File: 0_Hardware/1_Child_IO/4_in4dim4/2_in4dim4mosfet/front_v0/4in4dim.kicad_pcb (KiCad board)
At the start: 2 copper layers, 100.1 x 41.9 mm, 37 parts, among them IC1 ATTINY48-A, P1 CONN_8X2, P2 CONN_2, P3 CONN_2, P4 CONN_2, P5 CONN_2, Q1 PNP, Q2 PNP, Q3 PNP, Q4 PNP

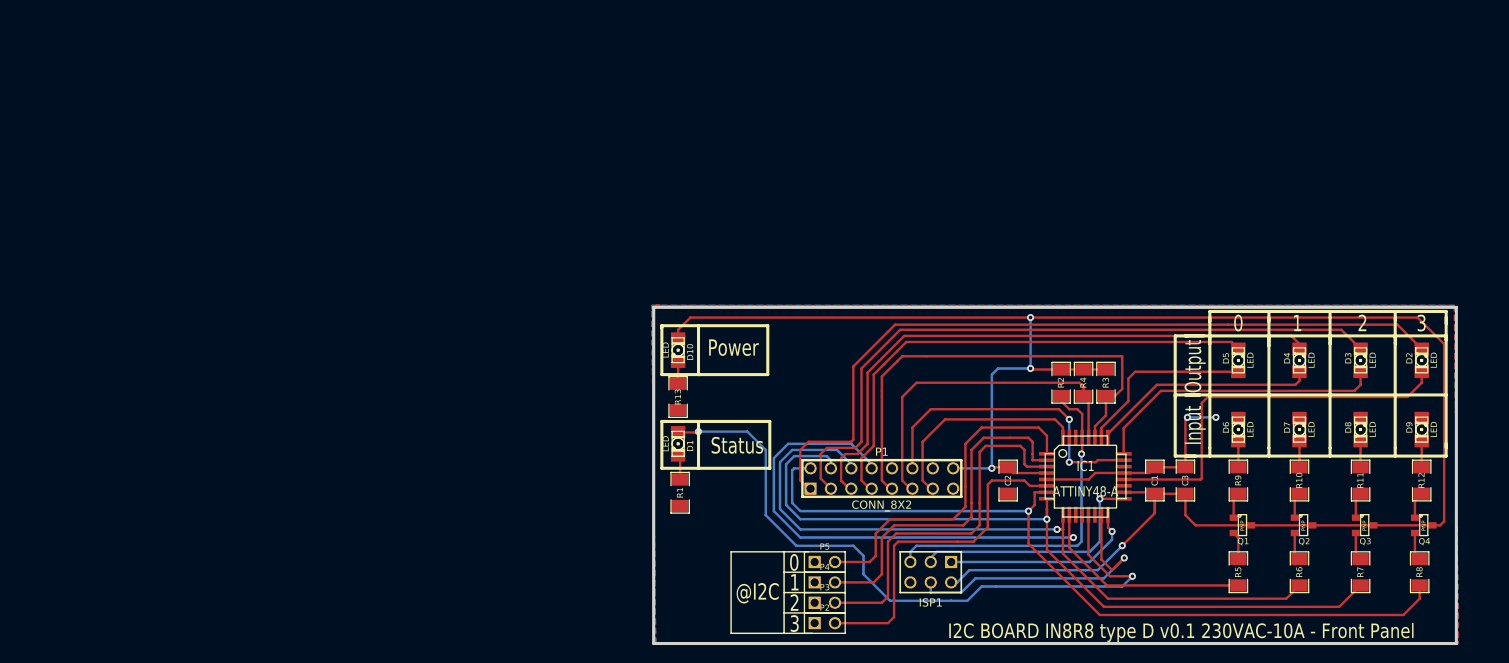
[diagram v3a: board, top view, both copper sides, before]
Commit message: MàJ du pcb front panel in4dim4 mosfet
Décalage vers la gauche des leds pawer status
Décalage vers le haut des cavaliers @I2C
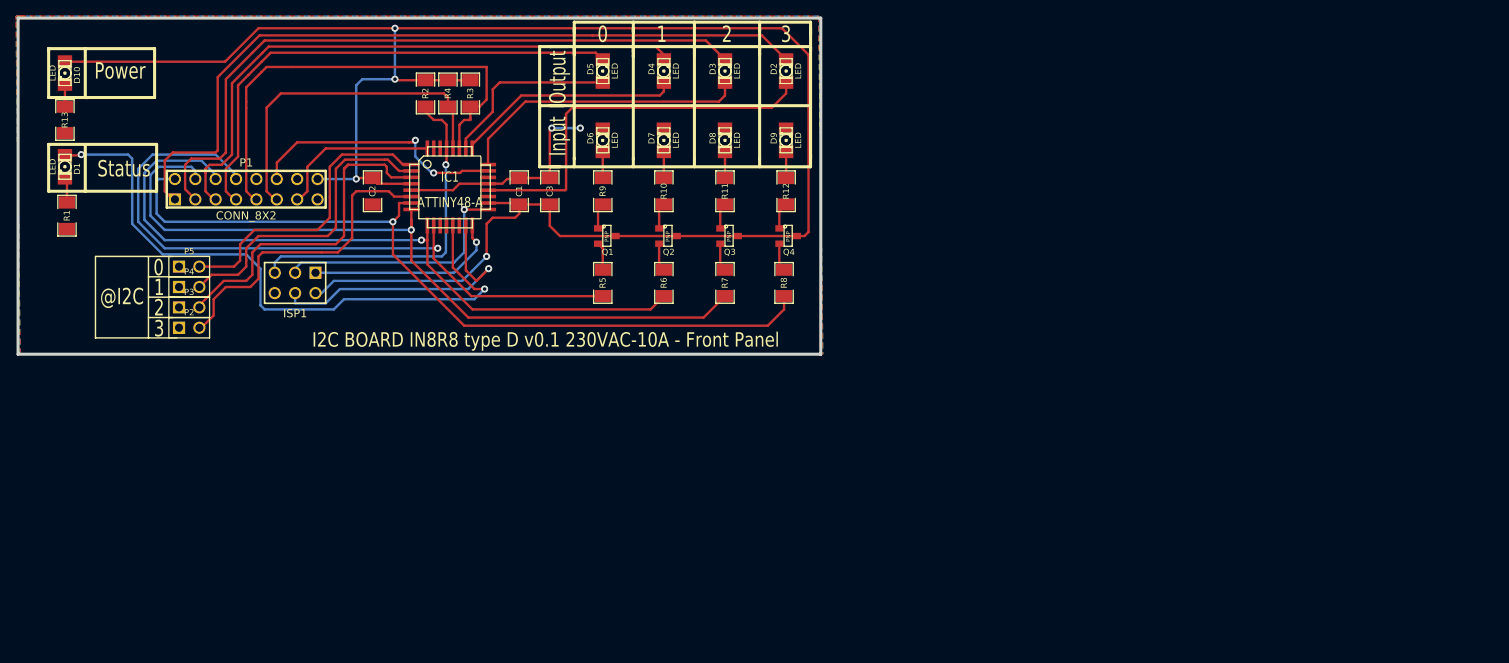
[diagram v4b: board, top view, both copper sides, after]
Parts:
- moved P2 87.4 mm to (123.7, 118.1)
- moved P3 87.4 mm to (123.7, 115.6)
- moved P4 87.4 mm to (123.7, 113.0)
- moved P5 87.4 mm to (123.7, 110.5)
- moved C2 87.1 mm to (146.6, 101.1)
- moved D5 87.1 mm to (175.3, 86.1)
- moved D6 87.1 mm to (175.3, 94.7)
- moved R4 87.1 mm to (156.0, 88.9)
- moved R5 87.1 mm to (175.3, 112.5)
- moved R9 87.1 mm to (175.3, 101.1)
- moved Q2 87.1 mm to (183.4, 106.7)
- moved Q4 87.1 mm to (198.4, 106.7)
- moved C1 87.1 mm to (164.8, 101.1)
- moved C3 87.1 mm to (168.7, 101.1)
- moved D2 87.1 mm to (198.1, 86.1)
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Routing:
- net ZC: track 26.9 -> 20.6 mm
- net /INT: track 38.3 -> 32.5 mm
- net LED: track 84.4 -> 79.2 mm
- net A1: track 44.0 -> 39.2 mm
- net A0: track 42.3 -> 37.6 mm
- net A2: track 46.0 -> 42.3 mm
- net +5V: track 242.7 -> 239.1 mm
- net A3: track 42.4 -> 39.7 mm

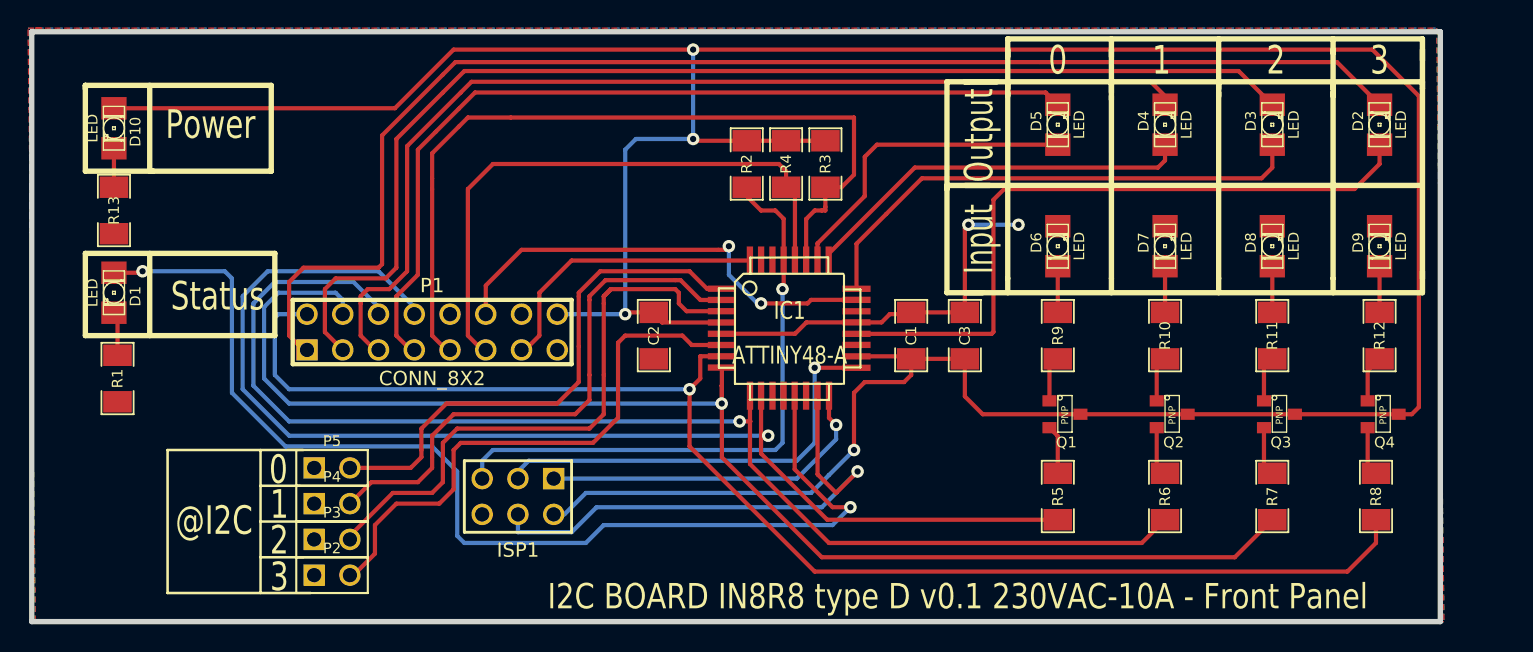
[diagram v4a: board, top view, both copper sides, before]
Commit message: mis à jour de la carte de puissance et de la front panel
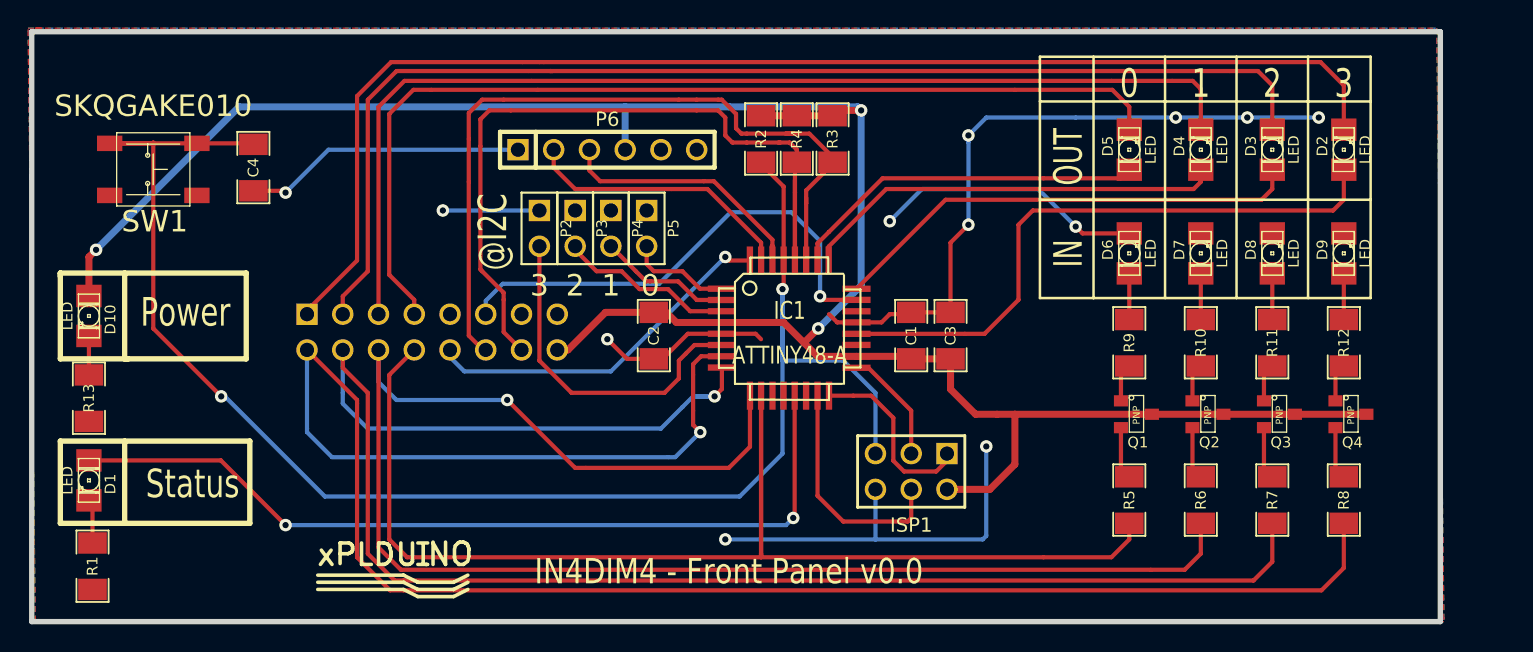
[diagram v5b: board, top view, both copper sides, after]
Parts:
- added C4: C, SM1206, F.Cu at (118.1, 89.2)
- added P6: CONN_6, PIN_ARRAY-6X1, F.Cu at (143.3, 87.9)
- added SW1: SKQGAKE010, SKQGAKE010, F.Cu at (111.0, 89.3)
- added logo_xplduino: VAL**, logo_xplduino, F.Cu at (128.0, 118.4)
- P1: moved to B.Cu
- moved P2 28.7 mm to (138.4, 93.5), turned to 270 degrees
- moved P5 28.1 mm to (146.1, 93.5), turned to 270 degrees
- moved P3 28.0 mm to (141.0, 93.5), turned to 270 degrees
- moved ISP1 28.0 mm to (164.8, 110.7)
- moved P4 27.8 mm to (143.5, 93.5), turned to 270 degrees
- moved D1 13.5 mm to (106.4, 111.4)
- moved R13 13.5 mm to (106.4, 105.5)
- moved D10 13.5 mm to (106.4, 99.7)
- moved R1 13.5 mm to (106.7, 117.5)
- moved D5 5.38 mm to (180.3, 87.9)
- moved D6 5.11 mm to (180.3, 95.2)
- moved R9 5.11 mm to (180.3, 101.6)
- moved R5 5.09 mm to (180.3, 112.8)
- moved Q1 5.08 mm to (180.8, 106.7)
- moved D2 3.10 mm to (195.6, 87.9)
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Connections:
- IC1 pad 11: SEL -> (no net)
- IC1 pad 12: N-0000047 -> (no net)
- IC1 pad 14: N-0000045 -> (no net)
- IC1 pad 19: N-0000044 -> (no net)
- IC1 pad 22: N-0000046 -> (no net)
- P1 pad 10: N-000003 -> ZC
- P1 pad 11: SCL -> /INT
- P1 pad 12: /INT -> SDA
- P1 pad 13: ZC -> (no net)
- P1 pad 14: N-000002 -> SCL
- P1 pad 9: SDA -> (no net)
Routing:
- net GND: track 27.8 -> 114.8 mm, vias 2 -> 11
- net RESET: track 43.0 -> 115.8 mm, vias 1 -> 2
- net +5V: track 239.1 -> 198.4 mm, vias 4 -> 3
- net CMD3: track 99.5 -> 133.7 mm
- net A0: track 37.6 -> 7.34 mm
- net A2: track 42.3 -> 12.5 mm
- net A1: track 39.2 -> 9.47 mm
- net CMD2: track 96.4 -> 119.2 mm
- net SCK: track 30.7 -> 8.20 mm, vias 1 -> 0
- net CMD1: track 90.3 -> 111.2 mm
- net MOSI: track 36.8 -> 16.7 mm, vias 1 -> 0
- net N-000004: track 0.00 -> 20.1 mm, vias 0 -> 1
- net TX: track 0.00 -> 19.5 mm
- net LED: track 79.2 -> 60.9 mm
- net RX: track 0.00 -> 18.1 mm
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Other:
- board text added: "IN"
- board text added: "IN4DIM4 - Front Panel v0.0"
- board text added: "OUT"
- board text removed: "3 2 1 0 ID 0 0 0 0 0 0 0 0 1 1 0 0 1 0 2 0 0 1 1 3 0 1 0 0 4 0 1 0 1 5 0 1 1 0 6 0 1 1 1 7 1 0 0 0 8 1 0 0 1 9 1 0 1 0 10 1 0 1 1 11 1 1 0 0 12 1 1 0 1 13 1 1 1 0 14 1 1 1 1 15"
- board text removed: "@I2C ID TABLE"
- board text removed: "I2C BOARD IN8R8 type D v0.1 230VAC-10A - Front Panel"
- board text removed: "Input"
- board text removed: "Output"

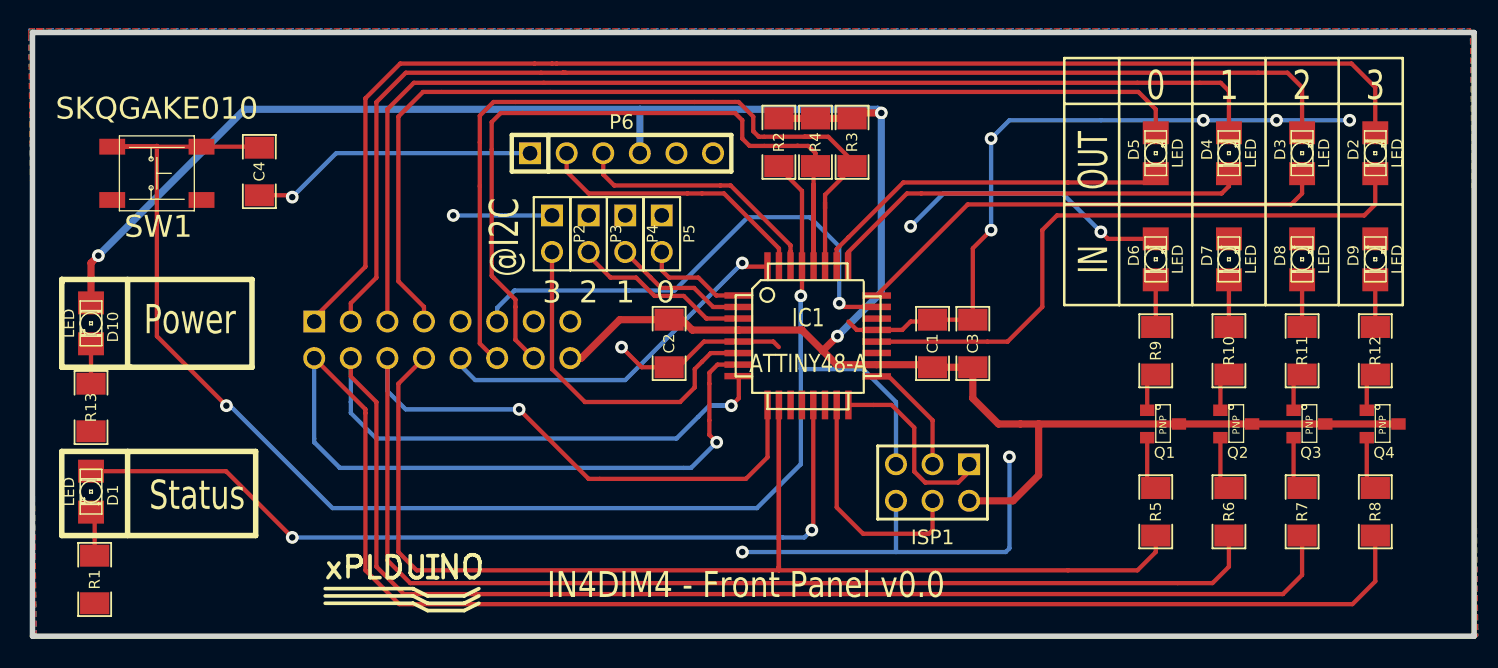
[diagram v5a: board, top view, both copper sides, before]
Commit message: Front panel dimmer: - passé tous les composants sauf leds et bouton reset face dessous pour libérer la place pour la sérigraphie - suite modif pinout connecteur 20 pins côté puissance - reroutage (TODO: à optimiser)
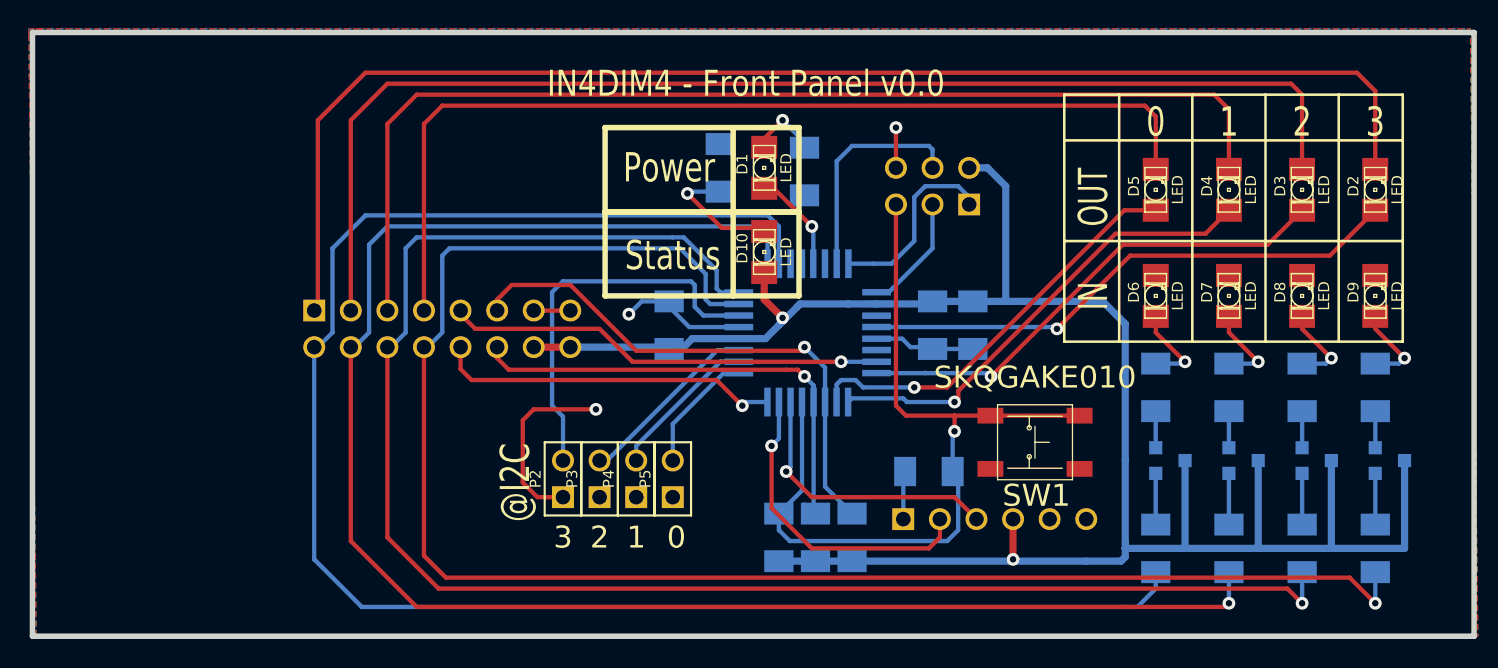
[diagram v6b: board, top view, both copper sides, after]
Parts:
- removed logo_xplduino: VAL**, logo_xplduino
- C1, C2, C3, C4, IC1, ISP1, P6, R1, R10, R11, R12, R13, R2, R3, R4, R5, R6, R7, R8, R9: moved to B.Cu
- Q1, Q2, Q3, Q4: footprint SOT23 -> SOT23EBC; moved to B.Cu
- moved SW1 63.8 mm to (172.0, 108.0)
- moved R1 56.8 mm to (156.0, 89.2)
- moved D1 51.9 mm to (153.2, 88.9), turned to 90 degrees
- moved C4 50.9 mm to (164.6, 110.0), turned to 0 degrees
- moved D10 47.0 mm to (153.2, 94.7), turned to 90 degrees
- moved R13 46.7 mm to (150.1, 88.9), turned to 90 degrees
- moved P6 36.3 mm to (169.2, 113.3)
- moved R2 27.4 mm to (154.2, 114.6), turned to 90 degrees
- moved R3 27.4 mm to (159.3, 114.6), turned to 90 degrees
- moved R4 27.4 mm to (156.7, 114.6), turned to 90 degrees
- moved ISP1 20.6 mm to (164.8, 90.2)
- moved P2 17.0 mm to (139.2, 110.5), turned to 90 degrees
- moved P3 17.0 mm to (141.7, 110.5), turned to 90 degrees
- moved P4 17.0 mm to (144.3, 110.5), turned to 90 degrees
- moved P5 17.0 mm to (146.8, 110.5), turned to 90 degrees
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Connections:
- P1 pad 11: /INT -> SDA
- P1 pad 12: SDA -> SCL
- P1 pad 13: (no net) -> GND
- P1 pad 14: SCL -> +5V
- P1 pad 2: CMD3 -> CMD0
- P1 pad 4: CMD2 -> CMD1
- P1 pad 6: CMD1 -> CMD2
- P1 pad 8: CMD0 -> CMD3
- P1 pad 9: (no net) -> /INT
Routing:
- net GND: track 114.8 -> 34.7 mm, vias 11 -> 3
- net RESET: track 115.8 -> 57.8 mm, vias 2 -> 1
- net LED: track 60.9 -> 7.03 mm, vias 2 -> 1
- net +5V: track 198.4 -> 146.2 mm, vias 3 -> 2
- net CMD0: track 91.9 -> 118.9 mm
- net SCL: track 56.6 -> 33.1 mm, vias 0 -> 1
- net CMD3: track 133.7 -> 114.5 mm
- net SDA: track 55.3 -> 37.6 mm, vias 0 -> 1
- net N-000005: track 20.1 -> 3.35 mm, vias 1 -> 0
- net _OUT0: track 44.1 -> 38.1 mm, vias 0 -> 1
- net N-0000017: track 2.77 -> 8.77 mm, vias 0 -> 1
- net CMD1: track 111.2 -> 116.9 mm
- net CMD2: track 119.2 -> 114.1 mm
- net /INT: track 34.8 -> 30.5 mm
- net _OUT3: track 25.5 -> 28.8 mm, vias 0 -> 1
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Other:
- net class GND: trace_width 0.50038 -> 0.254

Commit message: finalisation dimmer (front et back panel)
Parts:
- removed C4: C, SM1206
- added logo_xplduino: VAL**, logo_xplduino, F.Cu at (127.9, 84.3)
- ISP1: moved to F.Cu
- P6: value CONN_6 -> CONN_2; footprint PIN_ARRAY-6X1 -> PIN_ARRAY_2X1; moved to F.Cu
- moved P6 17.7 mm to (152.1, 108.5)
- moved SW1 7.44 mm to (165.2, 111.1)
- moved ISP1 0.57 mm to (165.1, 90.7), turned to 0 degrees
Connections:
- IC1 pad 10: CMD0 -> CMD2
- IC1 pad 11: (no net) -> CMD1
- IC1 pad 12: (no net) -> CMD0
- IC1 pad 23: /INT -> (no net)
- IC1 pad 7: CMD3 -> (no net)
- IC1 pad 8: CMD2 -> /INT
- IC1 pad 9: CMD1 -> CMD3
- P6 pad 1: N-000005 -> TX
- P6 pad 2: TX -> RX
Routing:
- net GND: track 34.7 -> 104.6 mm, vias 3 -> 14
- net TX: track 22.0 -> 5.79 mm, vias 1 -> 0
- net RX: track 19.5 -> 3.95 mm, vias 1 -> 0
- net RESET: track 57.8 -> 44.2 mm, vias 1 -> 2
- net SDA: track 37.6 -> 51.1 mm, vias 1 -> 0
- net SCL: track 33.1 -> 43.7 mm, vias 1 -> 0
- net +5V: track 146.2 -> 154.0 mm, vias 2 -> 1
- net MISO: track 13.2 -> 6.72 mm
- net /INT: track 30.5 -> 24.9 mm, vias 1 -> 0
- net CMD1: track 116.9 -> 121.3 mm
- net CMD0: track 118.9 -> 122.9 mm, vias 0 -> 1
- net MOSI: track 15.6 -> 11.8 mm
- net N-000005: track 3.35 -> 0.00 mm
- net N-000008: track 4.94 -> 7.97 mm
- net _OUT2: track 32.5 -> 35.3 mm
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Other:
- net class GND: trace_width 0.254 -> 0.50038
- board text added: "T-R"
- board text added: "reset"
